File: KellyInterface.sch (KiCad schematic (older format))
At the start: 39 parts

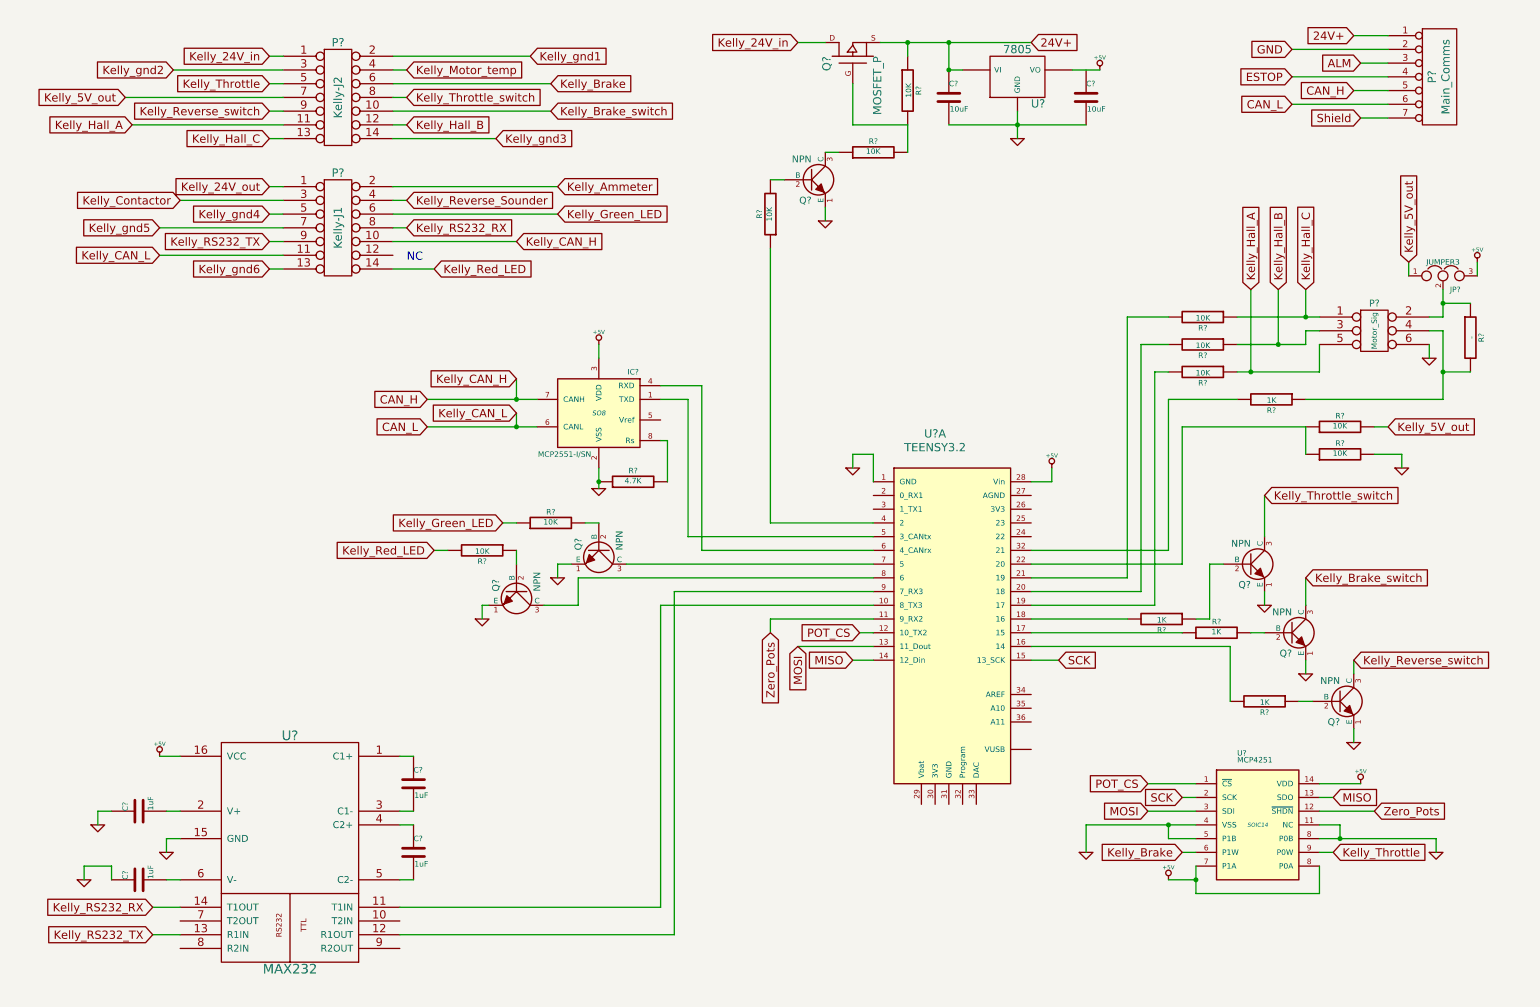
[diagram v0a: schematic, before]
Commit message: moved stops to new sheet
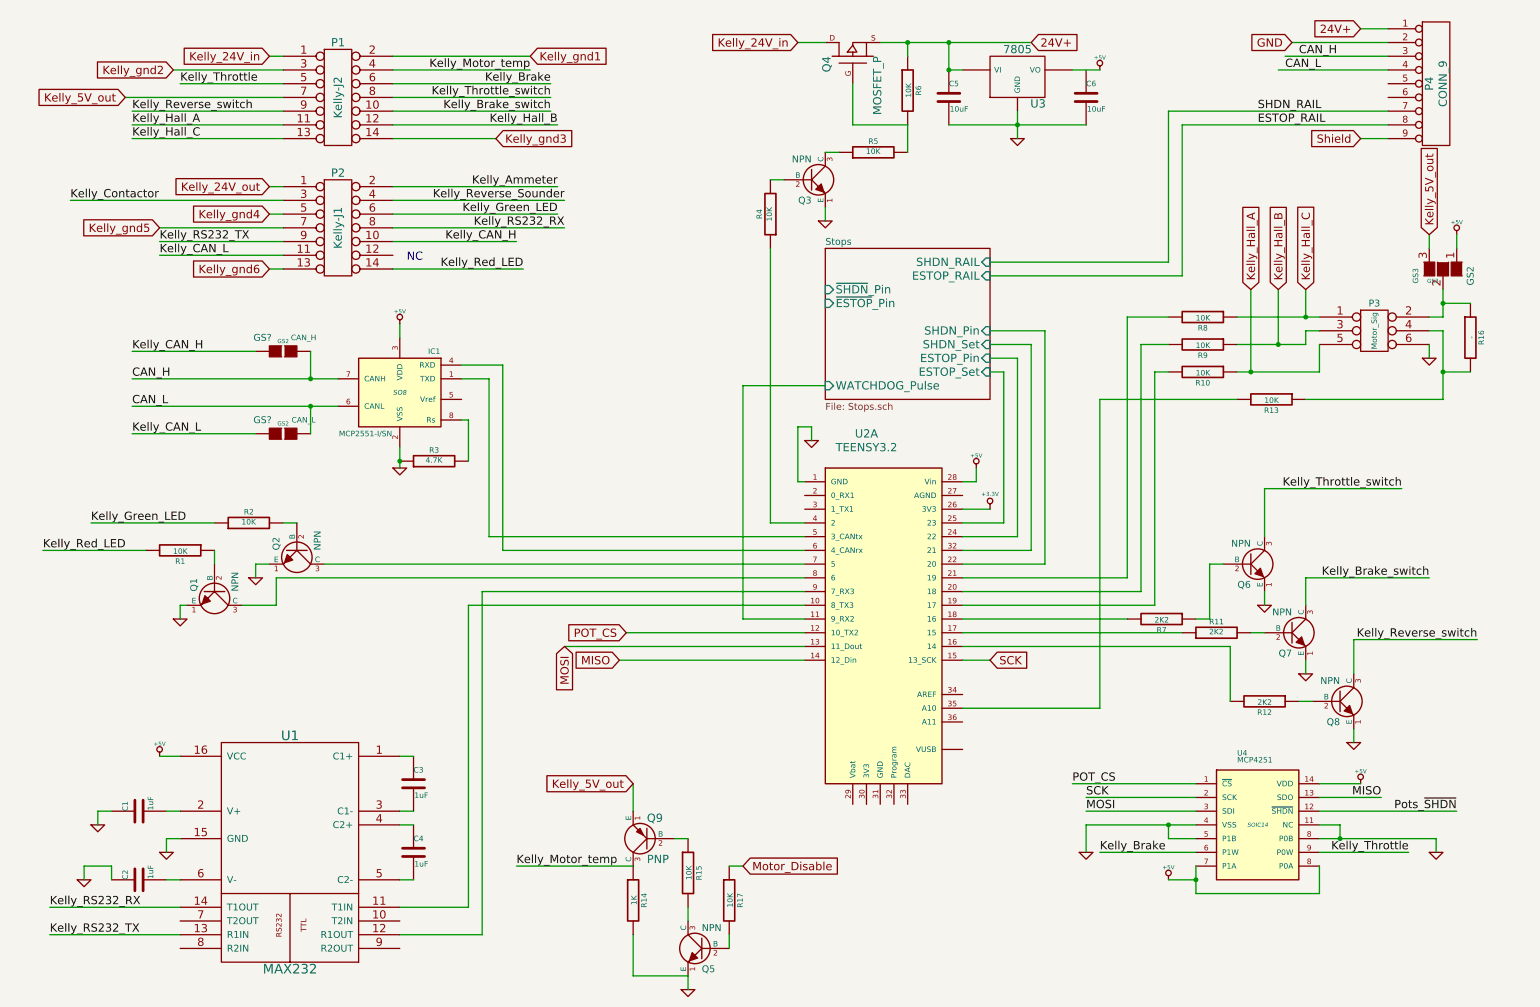
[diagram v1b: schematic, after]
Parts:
- removed JP?: JUMPER3, ~, symbol JUMPER3
- removed P?: Main_Comms, symbol CONN_7
- removed R? (x2): 10K, ~, symbol R
- added GS2: GS3, GS3, symbol GS3
- added GS?: CAN_H, GS2, symbol GS2
- added GS?: CAN_L, GS2, symbol GS2
- added P4: CONN_9, symbol CONN_9
- added Q5: NPN, ~, symbol NPN
- added Q9: PNP, ~, symbol PNP
- added R14: 1K, ~, symbol R
- added R15, R17: 10K, ~, symbol R
- R11, R12, R7: renamed from R?; value 1K -> 2K2
- R13: renamed from R?; value 1K -> 10K
- gave numbers to parts that had none: 31
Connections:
- net +5V: now also GS2.1 (G1)
- net 24V+: now also P4.1 (P1)
- net CAN_H: now also GS?.2 (G2), P4.3 (P3); no longer P2.10
- net CAN_L: now also GS?.2 (G2), P4.4 (P4); no longer P2.11
- net GND: now also P4.2 (P2), Q5.1 (E), R14.2
- net Kelly_5V_out: now also GS2.3 (G3), Q9.1 (E)
- net Kelly_Motor_temp: now also Q9.3 (C), R14.1
- net Shield: now also P4.9 (P9)
- net Stops/SHDN_Pin: now reaches U2.22 (20)
- net Stops/ESTOP_Pin: now reaches U2.24 (22)
- net Stops/ESTOP_Set: now reaches U2.25 (23)
- net +3.3V: now reaches U2.26 (3V3)
- net Stops/SHDN_Set: now reaches U2.32 (Program)
- net at R13.2: now also U2.35 (A10); no longer U2.32 (Program)
- net at P3.2, R16.1: now also GS2.2 (G2)
- net Zero_Pots renamed Pots_~SHDN~
- net Pots_~SHDN~: no longer U2.11 (9_RX2)
- new net: Q5.2 (B), R17.2
- new net: Q5.3 (C), R15.2
- new net: Q9.2 (B), R15.1
- new net ESTOP_RAIL: P4.8 (P8)
- new net Kelly_CAN_H: GS?.1 (G1), P2.10
- new net Kelly_CAN_L: GS?.1 (G1), P2.11
- new net Motor_Disable: R17.1
- new net SHDN_RAIL: P4.7 (P7)
- new net Stops/WATCHDOG_Pulse: U2.11 (9_RX2)
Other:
- moved on the sheet: IC1, Q1, Q2, R1, R2, R3, U2A

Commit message: Converted to Local and Hierarchical net labels
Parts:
- gave numbers to parts that had none: 2
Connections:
- net at Q4.G, R6.2: now also R5.1; no longer R5.2
- net at Q3.3 (C): now also R5.2; no longer R5.1
- net 24V+ renamed +24V
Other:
- moved on the sheet: C5, C6, GS1, GS3, IC1, P1, P2, Q3, Q4, Q5, Q9, R14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
